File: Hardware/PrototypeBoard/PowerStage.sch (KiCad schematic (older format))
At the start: 9 parts, among them Q1 IRF8721PBF-1, Q2 IRF8721PBF-1, Q3 IRF8721PBF-1, Q4 IRF8721PBF-1, Q5 IRF8721PBF-1, Q6 IRF8721PBF-1

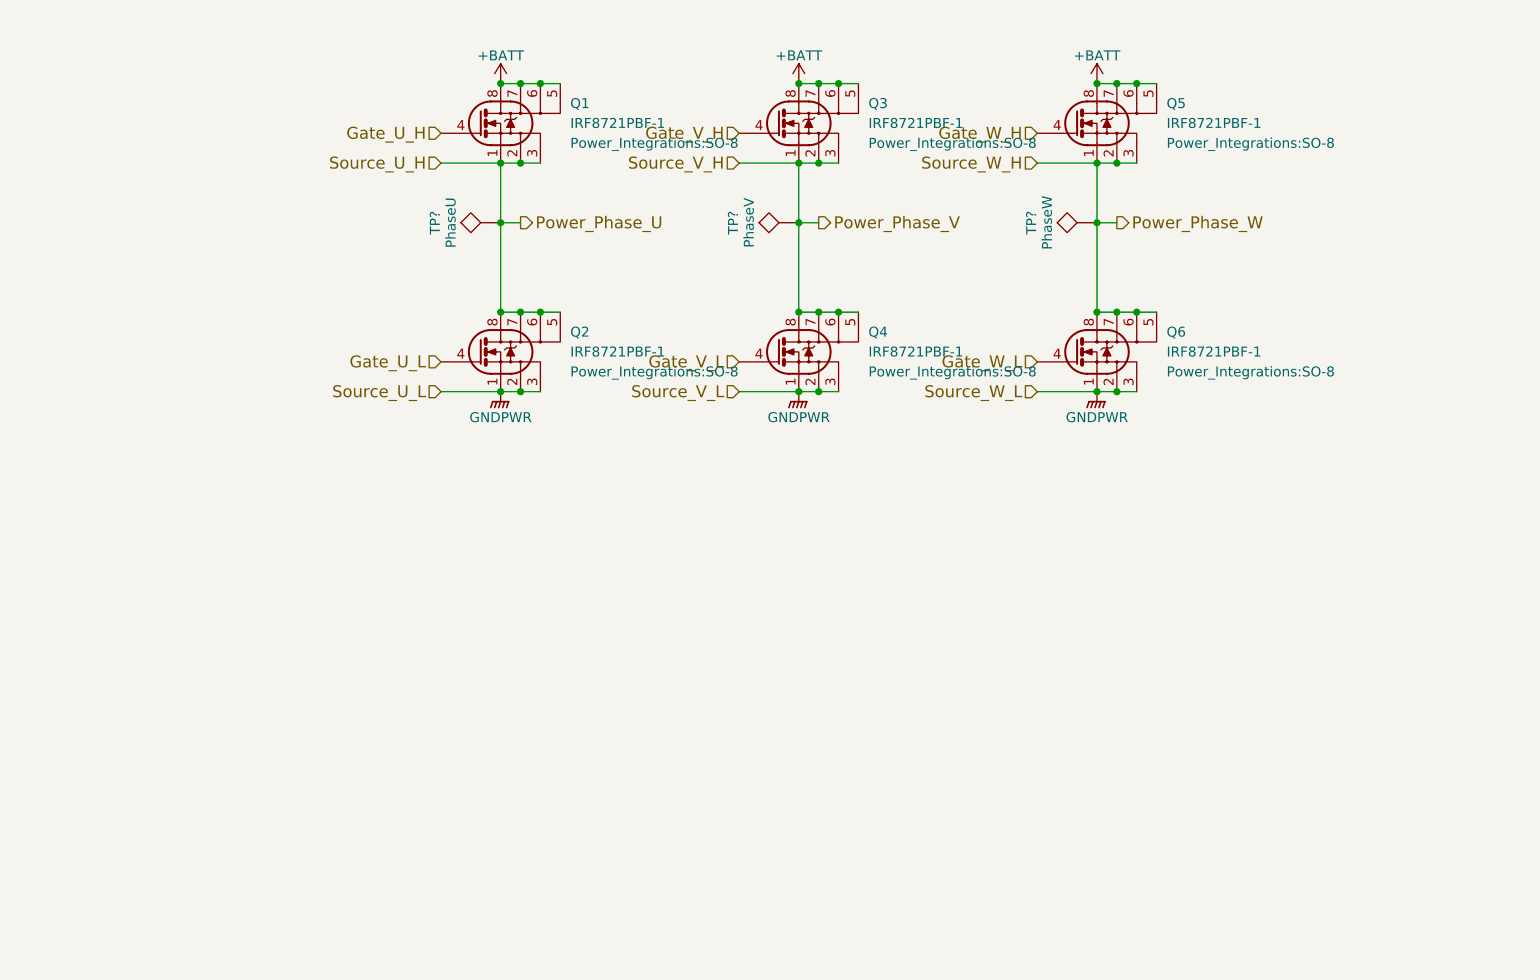
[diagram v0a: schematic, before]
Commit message: Fixed all ERC errors. Added power consumption estimation and other comments. Added links to datasheets. Dimensioned low pass and voltage dividers. Added TVS diodes for protection of voltage rails and ADC inputs. Added fuses. Added Testpoints. Added DC-link capacitors.
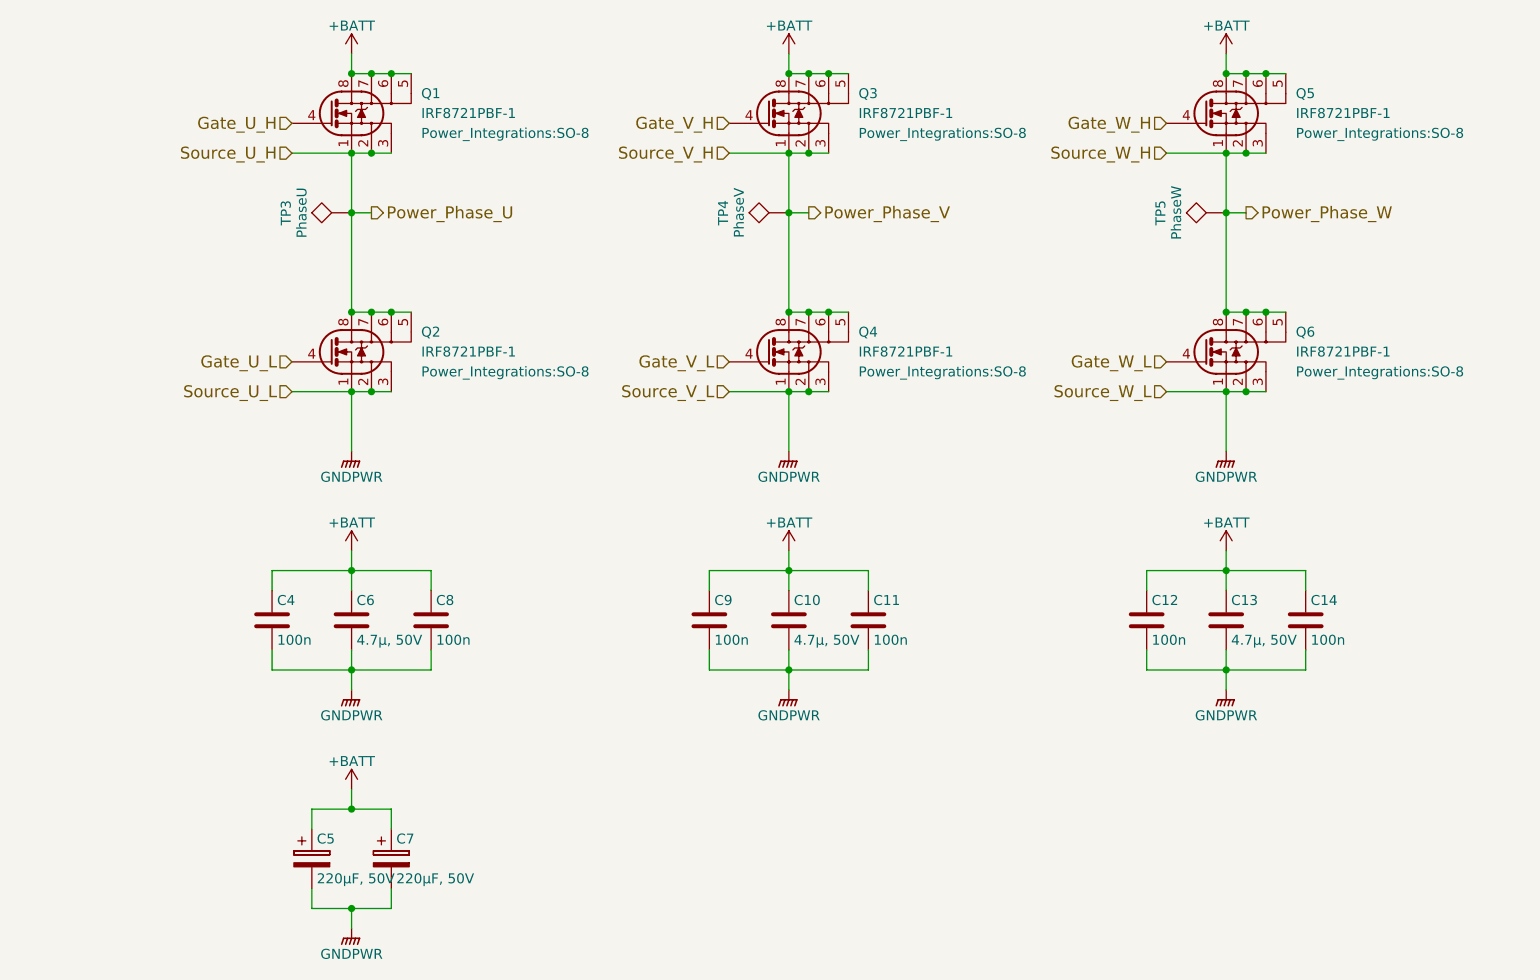
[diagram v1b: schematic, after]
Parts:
- added C10, C13, C6: 4.7μ, 50V, symbol C
- added C11, C12, C14, C4, C8, C9: 100n, symbol C
- added C5, C7: 220μF, 50V, symbol CP
- gave numbers to parts that had none: 3
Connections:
- net +BATT: now also C10.1, C11.1, C12.1, C13.1, C14.1, C4.1, C5.1, C6.1, C7.1, C8.1, C9.1
- net GNDPWR: now also C10.2, C11.2, C12.2, C13.2, C14.2, C4.2, C5.2, C6.2, C7.2, C8.2, C9.2
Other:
- moved on the sheet: Q1, Q2, Q3, Q4, Q5, Q6, TP3, TP4, TP5

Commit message: forgot files
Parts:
- C10, C11, C12, C13, C14, C4, C6, C8, C9: footprint (none) -> Capacitors_SMD:C_0805_HandSoldering
- C5, C7: footprint (none) -> Capacitors_SMD:CP_Elec_10x10
- Q1, Q2, Q3, Q4, Q5, Q6: footprint Power_Integrations:SO-8 -> libs:PG-TISON-8-1
- TP3, TP4, TP5: footprint (none) -> Measurement_Points:Measurement_Point_Round-TH_Big
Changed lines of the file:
@@
 F 0 "Q5" H 7850 2500 50  0000 L CNN
 F 1 "IRF8721PBF-1" H 7850 2400 50  0000 L CNN
-F 2 "Power_Integrations:SO-8" H 7850 2300 50  0000 L CNN
+F 2 "libs:PG-TISON-8-1" H 7850 2300 50  0000 L CNN
 F 3 "" H 7400 2400 50  0000 L CNN
 	1    7500 2400
@@
 F 0 "Q6" H 7850 3700 50  0000 L CNN
 F 1 "IRF8721PBF-1" H 7850 3600 50  0000 L CNN
-F 2 "Power_Integrations:SO-8" H 7850 3500 50  0000 L CNN
+F 2 "libs:PG-TISON-8-1" H 7850 3500 50  0000 L CNN
 F 3 "" H 7400 3600 50  0000 L CNN
 	1    7500 3600
@@
 F 0 "Q4" H 5650 3700 50  0000 L CNN
 F 1 "IRF8721PBF-1" H 5650 3600 50  0000 L CNN
-F 2 "Power_Integrations:SO-8" H 5650 3500 50  0000 L CNN
+F 2 "libs:PG-TISON-8-1" H 5650 3500 50  0000 L CNN
 F 3 "" H 5200 3600 50  0000 L CNN
 	1    5300 3600
@@
 F 0 "Q3" H 5650 2500 50  0000 L CNN
 F 1 "IRF8721PBF-1" H 5650 2400 50  0000 L CNN
-F 2 "Power_Integrations:SO-8" H 5650 2300 50  0000 L CNN
+F 2 "libs:PG-TISON-8-1" H 5650 2300 50  0000 L CNN
 F 3 "" H 5200 2400 50  0000 L CNN
 	1    5300 2400
@@
 F 0 "Q1" H 3450 2500 50  0000 L CNN
 F 1 "IRF8721PBF-1" H 3450 2400 50  0000 L CNN
-F 2 "Power_Integrations:SO-8" H 3450 2300 50  0000 L CNN
+F 2 "libs:PG-TISON-8-1" H 3450 2300 50  0000 L CNN
 F 3 "" H 3000 2400 50  0000 L CNN
 	1    3100 2400
@@
 F 0 "Q2" H 3450 3700 50  0000 L CNN
 F 1 "IRF8721PBF-1" H 3450 3600 50  0000 L CNN
-F 2 "Power_Integrations:SO-8" H 3450 3500 50  0000 L CNN
+F 2 "libs:PG-TISON-8-1" H 3450 3500 50  0000 L CNN
 F 3 "" H 3000 3600 50  0000 L CNN
 	1    3100 3600
@@
 F 0 "TP3" H 3100 3200 50  0000 C BNN
 F 1 "PhaseU" H 3100 3150 50  0000 C CNN
-F 2 "" H 3100 2900 50  0001 C CNN
+F 2 "Measurement_Points:Measurement_Point_Round-TH_Big" H 3100 2900 50  0001 C CNN
 F 3 "" H 3100 2900 50  0001 C CNN
 	1    3100 2900
@@
 F 0 "TP4" H 5300 3200 50  0000 C BNN
 F 1 "PhaseV" H 5300 3150 50  0000 C CNN
-F 2 "" H 5300 2900 50  0001 C CNN
+F 2 "Measurement_Points:Measurement_Point_Round-TH_Big" H 5300 2900 50  0001 C CNN
 F 3 "" H 5300 2900 50  0001 C CNN
 	1    5300 2900
@@
 F 0 "TP5" H 7500 3200 50  0000 C BNN
 F 1 "PhaseW" H 7500 3150 50  0000 C CNN
-F 2 "" H 7500 2900 50  0001 C CNN
+F 2 "Measurement_Points:Measurement_Point_Round-TH_Big" H 7500 2900 50  0001 C CNN
 F 3 "" H 7500 2900 50  0001 C CNN
 	1    7500 2900
@@
 F 0 "C6" H 3125 5050 50  0000 L CNN
 F 1 "4.7μ, 50V" H 3125 4850 50  0000 L CNN
-F 2 "" H 3138 4800 50  0001 C CNN
+F 2 "Capacitors_SMD:C_0805_HandSoldering" H 3138 4800 50  0001 C CNN
 F 3 "" H 3100 4950 50  0001 C CNN
 	1    3100 4950
@@
 F 0 "C8" H 3525 5050 50  0000 L CNN
 F 1 "100n" H 3525 4850 50  0000 L CNN
-F 2 "" H 3538 4800 50  0001 C CNN
+F 2 "Capacitors_SMD:C_0805_HandSoldering" H 3538 4800 50  0001 C CNN
 F 3 "" H 3500 4950 50  0001 C CNN
 	1    3500 4950
@@
 F 0 "C4" H 2725 5050 50  0000 L CNN
 F 1 "100n" H 2725 4850 50  0000 L CNN
-F 2 "" H 2738 4800 50  0001 C CNN
+F 2 "Capacitors_SMD:C_0805_HandSoldering" H 2738 4800 50  0001 C CNN
 F 3 "" H 2700 4950 50  0001 C CNN
 	1    2700 4950
@@
 F 0 "C5" H 2925 6250 50  0000 L CNN
 F 1 "220μF, 50V" H 2925 6050 50  0000 L CNN
-F 2 "" H 2938 6000 50  0001 C CNN
+F 2 "Capacitors_SMD:CP_Elec_10x10" H 2938 6000 50  0001 C CNN
 F 3 "" H 2900 6150 50  0001 C CNN
 	1    2900 6150
@@
 F 0 "C7" H 3325 6250 50  0000 L CNN
 F 1 "220μF, 50V" H 3325 6050 50  0000 L CNN
-F 2 "" H 3338 6000 50  0001 C CNN
+F 2 "Capacitors_SMD:CP_Elec_10x10" H 3338 6000 50  0001 C CNN
 F 3 "" H 3300 6150 50  0001 C CNN
 	1    3300 6150
@@
 F 0 "C9" H 4925 5050 50  0000 L CNN
 F 1 "100n" H 4925 4850 50  0000 L CNN
-F 2 "" H 4938 4800 50  0001 C CNN
+F 2 "Capacitors_SMD:C_0805_HandSoldering" H 4938 4800 50  0001 C CNN
 F 3 "" H 4900 4950 50  0001 C CNN
 	1    4900 4950
@@
 F 0 "C11" H 5725 5050 50  0000 L CNN
 F 1 "100n" H 5725 4850 50  0000 L CNN
-F 2 "" H 5738 4800 50  0001 C CNN
+F 2 "Capacitors_SMD:C_0805_HandSoldering" H 5738 4800 50  0001 C CNN
 F 3 "" H 5700 4950 50  0001 C CNN
 	1    5700 4950
@@
 F 0 "C12" H 7125 5050 50  0000 L CNN
 F 1 "100n" H 7125 4850 50  0000 L CNN
-F 2 "" H 7138 4800 50  0001 C CNN
+F 2 "Capacitors_SMD:C_0805_HandSoldering" H 7138 4800 50  0001 C CNN
 F 3 "" H 7100 4950 50  0001 C CNN
 	1    7100 4950
@@
 F 0 "C14" H 7925 5050 50  0000 L CNN
 F 1 "100n" H 7925 4850 50  0000 L CNN
-F 2 "" H 7938 4800 50  0001 C CNN
+F 2 "Capacitors_SMD:C_0805_HandSoldering" H 7938 4800 50  0001 C CNN
 F 3 "" H 7900 4950 50  0001 C CNN
 	1    7900 4950
@@
 F 0 "C10" H 5325 5050 50  0000 L CNN
 F 1 "4.7μ, 50V" H 5325 4850 50  0000 L CNN
-F 2 "" H 5338 4800 50  0001 C CNN
+F 2 "Capacitors_SMD:C_0805_HandSoldering" H 5338 4800 50  0001 C CNN
 F 3 "" H 5300 4950 50  0001 C CNN
 	1    5300 4950
@@
 F 0 "C13" H 7525 5050 50  0000 L CNN
 F 1 "4.7μ, 50V" H 7525 4850 50  0000 L CNN
-F 2 "" H 7538 4800 50  0001 C CNN
+F 2 "Capacitors_SMD:C_0805_HandSoldering" H 7538 4800 50  0001 C CNN
 F 3 "" H 7500 4950 50  0001 C CNN
 	1    7500 4950
